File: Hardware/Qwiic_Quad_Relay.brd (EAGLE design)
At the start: 82.5 x 47 mm, 125 parts, among them J2 Qwiic Right Angle, J3 Qwiic Right Angle, J4 POWER_JACK, J9 AVR_SPI_PROG_3X2TESTPOINTS, K1 RELAY-SPDT-JZC-11F, K2 RELAY-SPDT-JZC-11F, K3 RELAY-SPDT-JZC-11F, K4 RELAY-SPDT-JZC-11F, Q1 600mA/40V, Q2 600mA/40V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

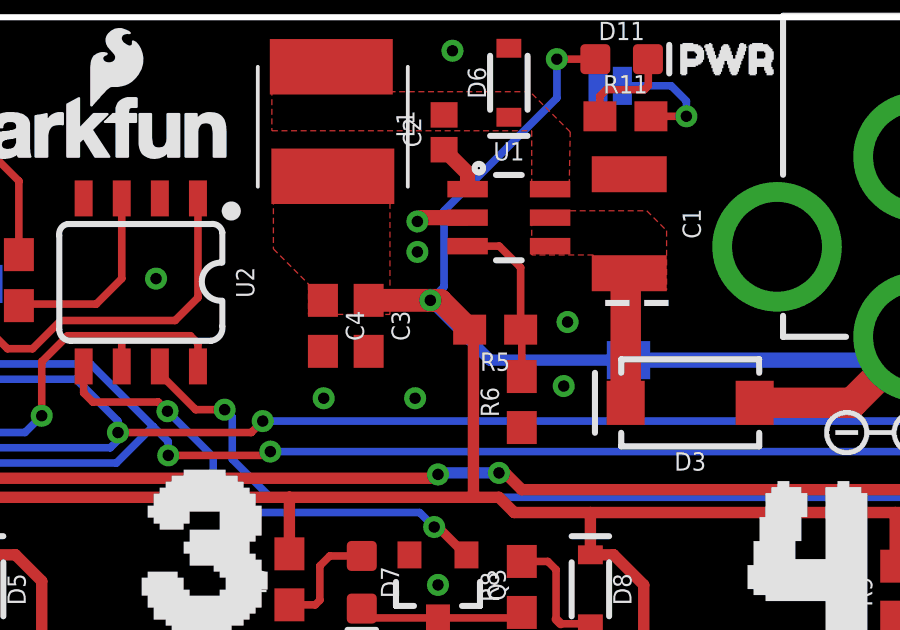
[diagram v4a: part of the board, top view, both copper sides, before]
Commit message: Fixes bypass
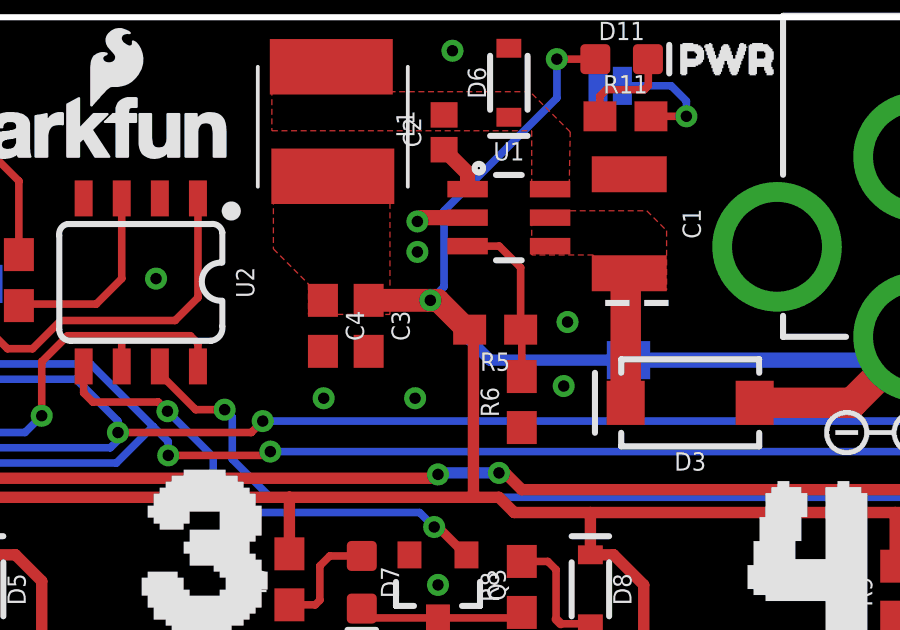
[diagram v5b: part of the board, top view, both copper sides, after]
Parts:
- renumbered JP1 to BYP
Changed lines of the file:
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@@
 <setting verticaltext="up"/>
 </settings>
-<grid distance="0.05" unitdist="inch" unit="inch" style="lines" multiple="1" display="yes" altdistance="0.002" altunitdist="inch" altunit="inch"/>
+<grid distance="0.05" unitdist="inch" unit="inch" style="lines" multiple="1" display="yes" altdistance="0.005" altunitdist="inch" altunit="inch"/>
 <layers>
 <layer number="1" name="Top" color="4" fill="1" visible="yes" active="yes"/>
@@
 <layer number="37" name="tTest" color="7" fill="1" visible="no" active="yes"/>
 <layer number="38" name="bTest" color="7" fill="1" visible="no" active="yes"/>
-<layer number="39" name="tKeepout" color="4" fill="11" visible="yes" active="yes"/>
+<layer number="39" name="tKeepout" color="4" fill="11" visible="no" active="yes"/>
 <layer number="40" name="bKeepout" color="1" fill="11" visible="no" active="yes"/>
-<layer number="41" name="tRestrict" color="4" fill="10" visible="yes" active="yes"/>
+<layer number="41" name="tRestrict" color="4" fill="10" visible="no" active="yes"/>
 <layer number="42" name="bRestrict" color="1" fill="10" visible="no" active="yes"/>
 <layer number="43" name="vRestrict" color="2" fill="10" visible="no" active="yes"/>
@@
 <attribute name="VALUE" x="60.3504" y="45.847" size="0.6096" layer="28" font="vector" ratio="20" rot="MR180" align="top-center"/>
 </element>
-<element name="JP1" library="SparkFun-Jumpers" package="SMT-JUMPER_2_NO_SILK" package3d_urn="urn:adsk.eagle:package:39279/1" value="JUMPER-SMT_2_NO_SILK" x="60.96" y="35.56" smashed="yes" rot="MR0">
+<element name="BYP" library="SparkFun-Jumpers" package="SMT-JUMPER_2_NO_SILK" package3d_urn="urn:adsk.eagle:package:39279/1" value="JUMPER-SMT_2_NO_SILK" x="60.96" y="35.56" smashed="yes" rot="MR0">
 <attribute name="NAME" x="60.96" y="36.703" size="0.6096" layer="26" font="vector" ratio="20" rot="MR0" align="bottom-center"/>
 <attribute name="VALUE" x="60.96" y="34.417" size="0.6096" layer="28" font="vector" ratio="20" rot="MR0" align="top-center"/>
@@
 <contactref element="D10" pad="C"/>
 <contactref element="L1" pad="P2"/>
-<contactref element="R5" pad="2"/>
 <contactref element="C3" pad="1"/>
 <contactref element="C4" pad="1"/>
-<wire x1="55.665" y1="36.576" x2="55.792" y2="36.449" width="0.381" layer="1"/>
 <wire x1="55.792" y1="36.449" x2="55.792" y2="30.988" width="0.381" layer="1"/>
-<wire x1="55.665" y1="36.576" x2="54.688" y2="37.553" width="0.762" layer="1"/>
-<wire x1="54.688" y1="37.553" x2="54.356" y2="37.553" width="0.762" layer="1"/>
 <contactref element="R1" pad="2"/>
 <contactref element="R3" pad="2"/>
 <contactref element="R7" pad="2"/>
 <contactref element="R9" pad="2"/>
+<wire x1="54.61" y1="37.553" x2="54.356" y2="37.553" width="0.762" layer="1"/>
 <wire x1="54.356" y1="37.553" x2="52.2986" y2="37.553" width="0.762" layer="1"/>
 <wire x1="9.779" y1="31.115" x2="19.05" y2="31.115" width="0.381" layer="1"/>
@@
 <wire x1="55.792" y1="30.988" x2="49.657" y2="30.988" width="0.381" layer="1"/>
 <wire x1="9.017" y1="30.352996875" x2="9.017" y2="28.9766" width="0.381" layer="1"/>
-<contactref element="JP1" pad="2"/>
+<contactref element="BYP" pad="2"/>
 <wire x1="60.5536" y1="35.56" x2="56.349" y2="35.56" width="0.381" layer="16"/>
 <wire x1="56.349" y1="35.56" x2="54.356" y2="37.553" width="0.381" layer="16"/>
@@
 <vertex x="53.0098" y="42.545"/>
 </polygon>
+<contactref element="R5" pad="2"/>
+<wire x1="55.665" y1="36.576" x2="55.587" y2="36.576" width="0.762" layer="1"/>
+<wire x1="55.587" y1="36.576" x2="54.61" y2="37.553" width="0.762" layer="1"/>
+<wire x1="55.665" y1="36.576" x2="55.792" y2="36.449" width="0" layer="19" extent="1-1"/>
 </signal>
 <signal name="VIN">
@@
 <wire x1="65.1674" y1="34.1376" x2="68.4116" y2="34.1376" width="1.016" layer="1"/>
 <wire x1="68.4116" y1="34.1376" x2="70.612" y2="36.338" width="1.016" layer="1"/>
-<contactref element="JP1" pad="1"/>
+<contactref element="BYP" pad="1"/>
 <wire x1="69.834" y1="35.56" x2="61.3664" y2="35.56" width="0.508" layer="16"/>
 <wire x1="70.612" y1="36.338" x2="69.834" y2="35.56" width="0.508" layer="16"/>

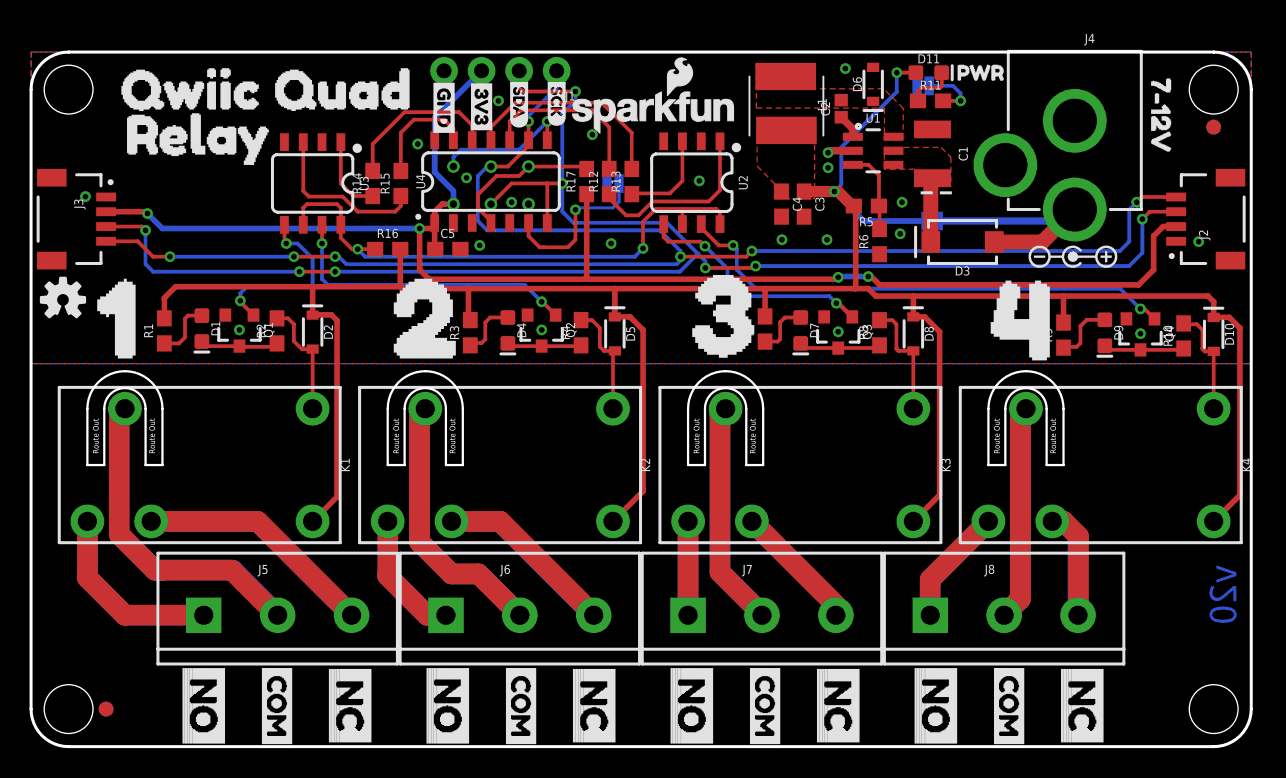
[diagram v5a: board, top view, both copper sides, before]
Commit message: Adds better silk, additional standoff, schotkky diode to protect dc/dc converter circuit
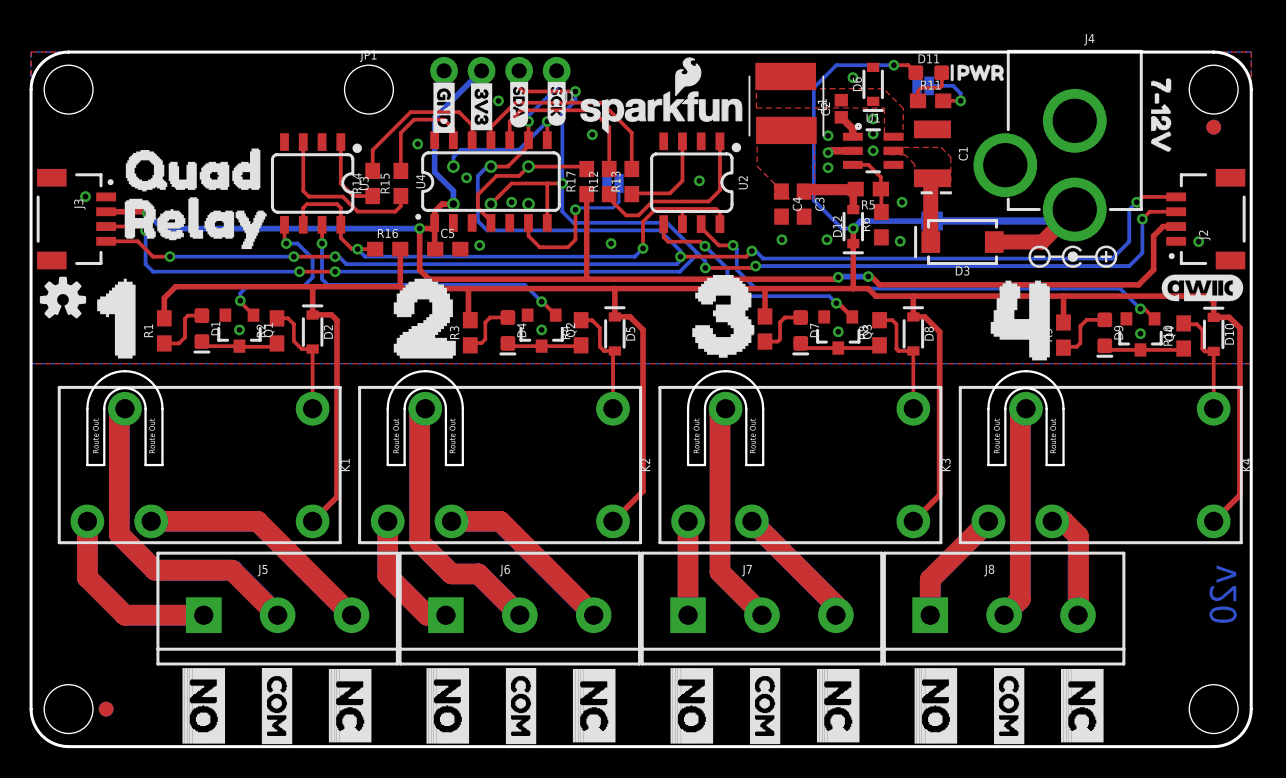
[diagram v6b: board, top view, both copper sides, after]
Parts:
- removed LOGO3: SFE_LOGO_NAME_FLAME.1_INCH, SparkFun-Aesthetics:SFE_LOGO_NAME_FLAME_.1
- removed U$50: (no value), 5V Wall Adapter:5V_WALL_ADAPTER0
- removed U$52: (no value), jumper:JUMPER0
- added D12: 3A/10V/280mV, SparkFun-DiscreteSemi:SOD-323
- added JP1: STAND-OFF, SparkFun-Hardware:STAND-OFF
- added U$55: (no value), SparkFun-Aesthetics:QWIIC_5.5MM
- added U$57: (no value), SparkFun-Aesthetics:SFE_LOGO_NAME_FLAME_.2
- U$43, U$6: device Quad:QWIIC_QUAD_0 -> Quad:QUAD0
- U$53: device SparkFun-Buzzard:LED_32 -> SparkFun-Buzzard:LED
- moved U$43 13.3 mm to (37.1, 34.5)
- moved U$44 10.4 mm to (25.9, 34.6)
- moved U$7 5.69 mm to (4.04, 35.7)
- moved U$6 5.44 mm to (4.01, 39.0)
- moved R5 1.15 mm to (56.6, 37.7)
- moved R6 1.15 mm to (57.5, 35.3)
- moved U$42 1.09 mm to (79.6, 29.0)
- moved LOGO1 0.56 mm to (42.7, 42.9)
- moved U$53 0.21 mm to (62.6, 42.7)
- renumbered JP2 to LED, JP3 to ADR
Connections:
- new net 5V_OUT: C3.1, C4.1, D12.A, L1.P2, R5.2
- net 5V: now also D12.C; no longer C3.1, C4.1, L1.P2, R5.2
- net VIN_DC_DC: no longer U1.4
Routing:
- net 5V_OUT: track 0.00 -> 5.02 mm
- net FB: track 5.71 -> 4.62 mm
- net 5V: track 178.9 -> 179.6 mm
- net GND: vias 21 -> 25
- added copper zone on layer 1, net 5V_OUT
- removed copper zone on layer 1, net 5V

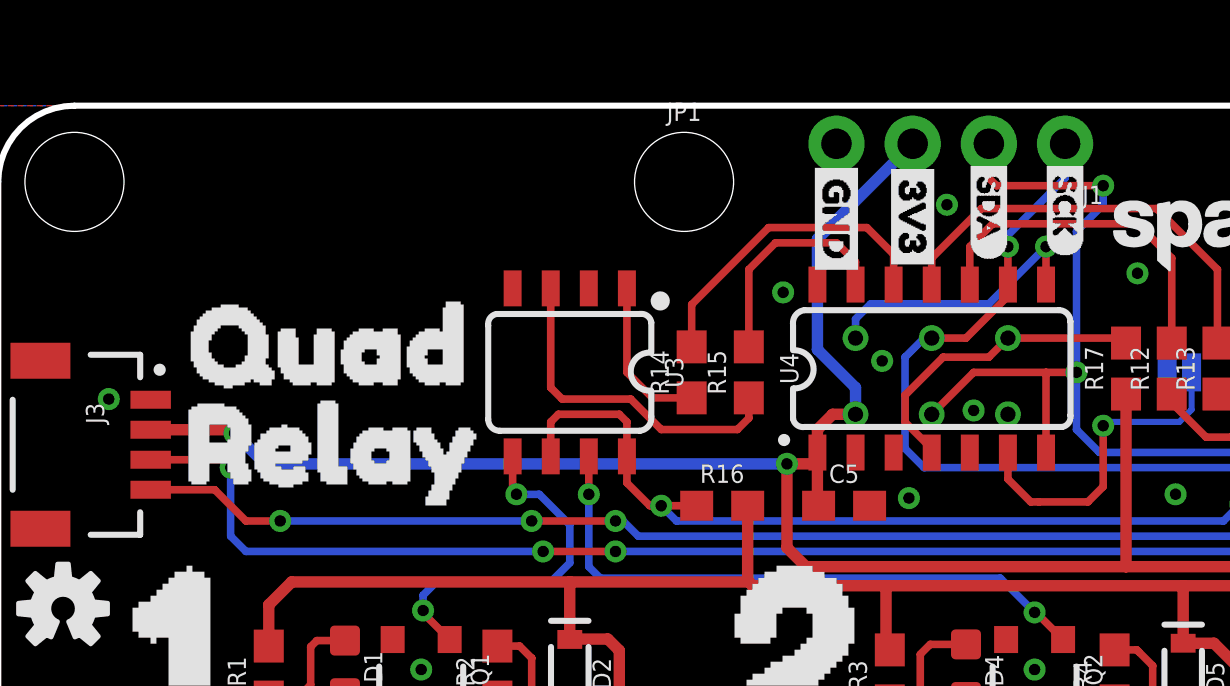
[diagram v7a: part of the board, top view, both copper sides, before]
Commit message: Adds silk to indicate qwiic board standoffs
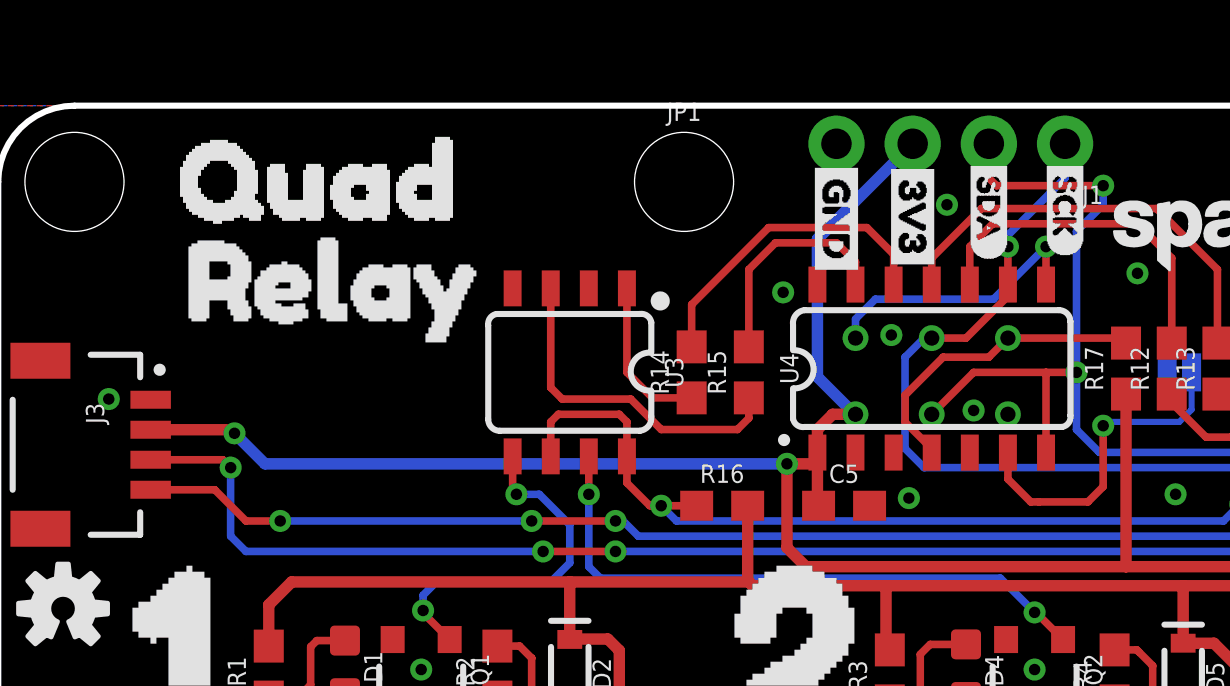
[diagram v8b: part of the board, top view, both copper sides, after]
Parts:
- added U$50: (no value), standoff_text:STANDOFFS0
- added U$52: (no value), standoff_text:FOR1
- added U$58: (no value), standoff_text:QWIIC_BOARD2
- moved U$6 5.50 mm to (3.66, 44.5)
- moved U$7 5.44 mm to (4.04, 41.1)
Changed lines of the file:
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@@
 <layer number="37" name="tTest" color="7" fill="1" visible="no" active="yes"/>
 <layer number="38" name="bTest" color="7" fill="1" visible="no" active="yes"/>
-<layer number="39" name="tKeepout" color="4" fill="11" visible="yes" active="yes"/>
+<layer number="39" name="tKeepout" color="4" fill="11" visible="no" active="yes"/>
 <layer number="40" name="bKeepout" color="1" fill="11" visible="no" active="yes"/>
 <layer number="41" name="tRestrict" color="4" fill="10" visible="no" active="yes"/>
@@
 <layer number="45" name="Holes" color="7" fill="1" visible="yes" active="yes"/>
 <layer number="46" name="Milling" color="3" fill="1" visible="no" active="yes"/>
-<layer number="47" name="Measures" color="7" fill="1" visible="yes" active="yes"/>
+<layer number="47" name="Measures" color="7" fill="1" visible="no" active="yes"/>
 <layer number="48" name="Document" color="7" fill="1" visible="no" active="yes"/>
 <layer number="49" name="Reference" color="13" fill="1" visible="yes" active="yes"/>
@@
 <layer number="115" name="ReferenceISLANDS" color="7" fill="1" visible="no" active="no"/>
 <layer number="116" name="Patch_BOT" color="9" fill="4" visible="no" active="no"/>
-<layer number="117" name="PM_Ref" color="26" fill="1" visible="yes" active="yes"/>
+<layer number="117" name="PM_Ref" color="26" fill="1" visible="no" active="yes"/>
 <layer number="118" name="Rect_Pads" color="7" fill="1" visible="no" active="no"/>
-<layer number="119" name="PF_Ref" color="31" fill="1" visible="yes" active="yes"/>
-<layer number="120" name="WFL_Ref" color="25" fill="1" visible="yes" active="yes"/>
+<layer number="119" name="PF_Ref" color="31" fill="1" visible="no" active="yes"/>
+<layer number="120" name="WFL_Ref" color="25" fill="1" visible="no" active="yes"/>
 <layer number="121" name="_tsilk" color="7" fill="1" visible="no" active="no"/>
 <layer number="122" name="_bsilk" color="7" fill="1" visible="no" active="no"/>
@@
 <element name="J1" library="SparkFun-Connectors" package="1X04_NO_SILK" value="" x="35.56" y="45.72" smashed="yes" rot="R180">
 <attribute name="NAME" x="36.83" y="44.323" size="0.6096" layer="25" font="vector" ratio="20" rot="R180"/>
-<attribute name="PROD_ID" value="CONN-09696" x="35.56" y="45.72" size="1.778" layer="27" font="vector" ratio="15" rot="R180" display="off"/>
 <attribute name="VALUE" x="36.83" y="47.752" size="0.6096" layer="27" font="vector" ratio="20" rot="R180"/>
 </element>
@@
 <element name="U$4" library="3" package="30" value="" x="40.132" y="29.21" smashed="yes"/>
 <element name="U$5" library="4" package="40" value="" x="60.325" y="28.829" smashed="yes"/>
-<element name="U$7" library="relay" package="RELAY0" value="" x="4.0386" y="35.7124" smashed="yes"/>
+<element name="U$7" library="relay" package="RELAY0" value="" x="4.0386" y="41.148" smashed="yes"/>
 <element name="LOGO2" library="SparkFun-Aesthetics" package="OSHW-LOGO-S" value="OSHW-LOGOS" x="2.159" y="30.226" smashed="yes"/>
 <element name="U$15" library="NO" package="NO0" value="" x="11.684" y="6.223" smashed="yes" rot="R270"/>
@@
 </element>
 <element name="U$55" library="SparkFun-Aesthetics" package="QWIIC_5.5MM" value="" x="79.248" y="31.0388" smashed="yes"/>
-<element name="U$6" library="Quad" package="QUAD0" value="" x="4.0132" y="39.0144" smashed="yes"/>
+<element name="U$6" library="Quad" package="QUAD0" value="" x="3.6576" y="44.5008" smashed="yes"/>
 <element name="U$43" library="Quad" package="QUAD0" value="" x="37.1348" y="34.544" smashed="yes" rot="MR0"/>
 <element name="U$53" library="SparkFun-Buzzard" package="LED" value="" x="62.5856" y="42.672" smashed="yes" rot="MR0"/>
 <element name="U$57" library="SparkFun-Aesthetics" package="SFE_LOGO_NAME_FLAME_.2" value="" x="48.1076" y="34.1376" smashed="yes" rot="MR0"/>
+<element name="U$50" library="standoff_text" package="STANDOFFS0" value="" x="17.6276" y="45.5168" smashed="yes" rot="MR0"/>
+<element name="U$52" library="standoff_text" package="FOR1" value="" x="15.1384" y="43.688" smashed="yes" rot="MR0"/>
+<element name="U$58" library="standoff_text" package="QWIIC_BOARD2" value="" x="18.542" y="41.8592" smashed="yes" rot="MR0"/>
 </elements>
 <signals>
@@
 <via x="45.212" y="38.2778" extent="1-16" drill="0.381"/>
 <via x="31.623" y="43.688" extent="1-16" drill="0.381"/>
-<via x="29.464" y="38.481" extent="1-16" drill="0.381"/>
+<via x="29.7688" y="39.3446" extent="1-16" drill="0.381"/>
 <via x="26.162" y="40.767" extent="1-16" drill="0.381"/>
 <via x="32.512" y="36.83" extent="1-16" drill="0.381"/>
@@
 <wire x1="26.289" y1="35.052" x2="8.89" y2="35.052" width="0.381" layer="16"/>
 <contactref element="J9" pad="2"/>
-<wire x1="28.575" y1="37.592" x2="27.305" y2="38.862" width="0.381" layer="16"/>
-<wire x1="27.305" y1="42.545" x2="27.305" y2="38.862" width="0.381" layer="16"/>
-<wire x1="28.575" y1="36.703" x2="28.575" y2="37.592" width="0.381" layer="16"/>
+<wire x1="28.575" y1="36.703" x2="28.5496" y2="36.703" width="0.381" layer="16"/>
+<wire x1="28.5496" y1="36.703" x2="27.305" y2="37.9476" width="0.381" layer="16"/>
+<wire x1="27.305" y1="42.545" x2="27.305" y2="37.9476" width="0.381" layer="16"/>
 <wire x1="30.48" y1="45.72" x2="27.305" y2="42.545" width="0.381" layer="16"/>
 <wire x1="75.946" y1="32.258" x2="74.93" y2="31.242" width="0.381" layer="1"/>
@@
 <contactref element="U4" pad="8"/>
 <via x="34.925" y="42.291" extent="1-16" drill="0.381"/>
-<wire x1="34.925" y1="42.291" x2="33.02" y2="40.386" width="0.254" layer="16"/>
-<wire x1="33.02" y1="40.386" x2="29.083" y2="40.386" width="0.254" layer="16"/>
-<wire x1="29.083" y1="40.386" x2="28.575" y2="39.878" width="0.254" layer="16"/>
+<wire x1="34.925" y1="42.291" x2="33.1724" y2="40.5384" width="0.254" layer="16"/>
+<wire x1="33.1724" y1="40.5384" x2="29.2354" y2="40.5384" width="0.254" layer="16"/>
+<wire x1="29.2354" y1="40.5384" x2="28.575" y2="39.878" width="0.254" layer="16"/>
 <wire x1="28.575" y1="39.878" x2="28.575" y2="39.243" width="0.254" layer="16"/>
 <wire x1="34.925" y1="41.027" x2="34.925" y2="42.291" width="0.254" layer="1"/>
